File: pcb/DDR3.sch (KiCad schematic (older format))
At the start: 3 parts

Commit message: schematic completed. Time for review
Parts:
- added R?: 100, symbol R
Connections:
- net DDR3_CK_N: now also R?.2
- net DDR3_CK_P: now also R?.1
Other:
- moved on the sheet: R?, U?A

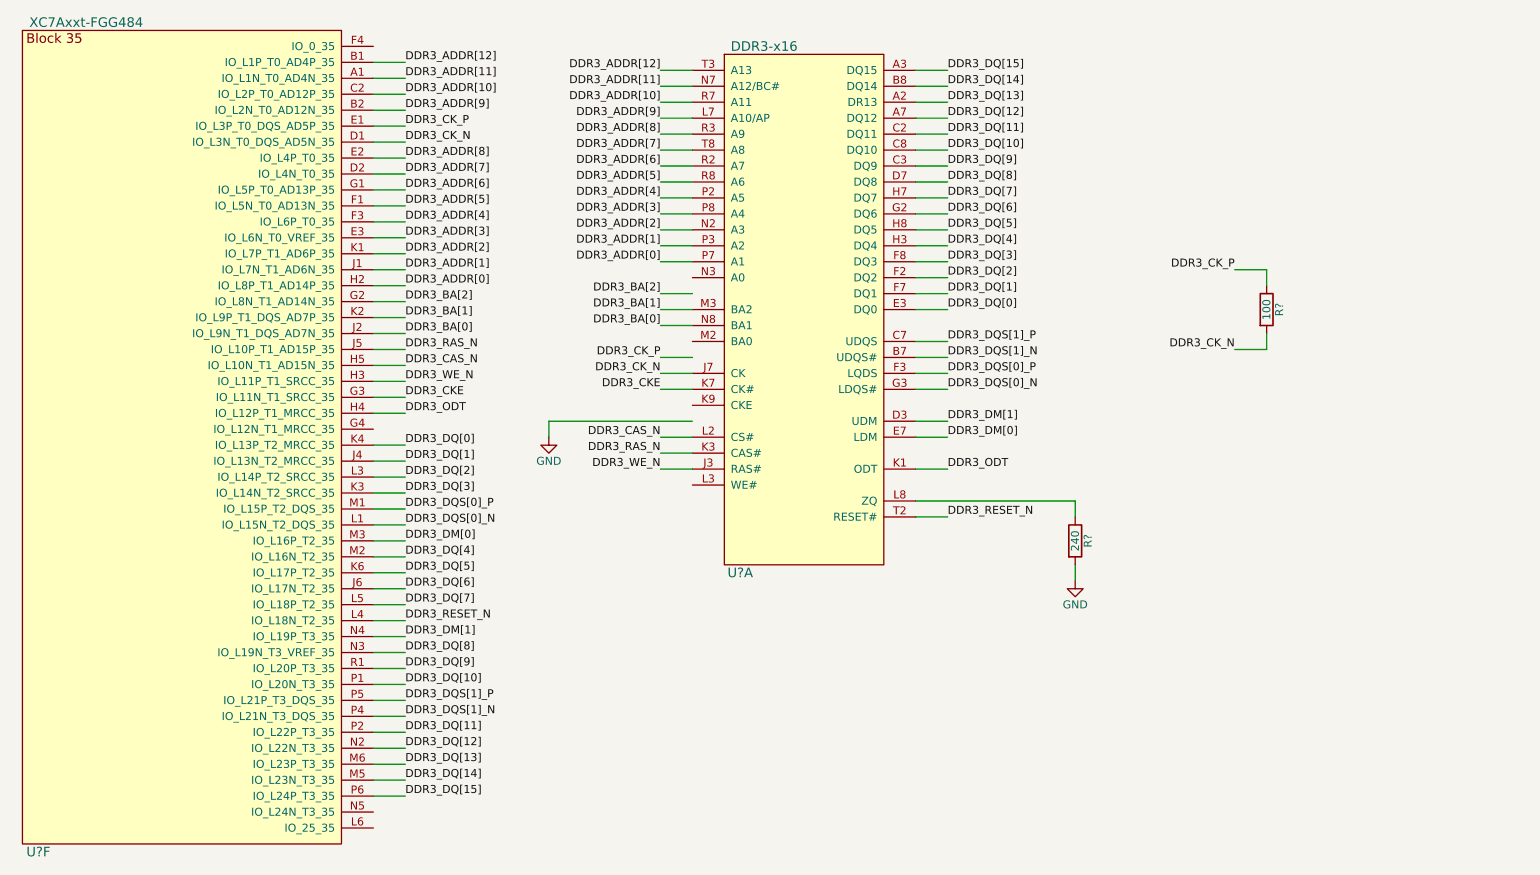
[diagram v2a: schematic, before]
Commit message: Added part numbers and updated schematic
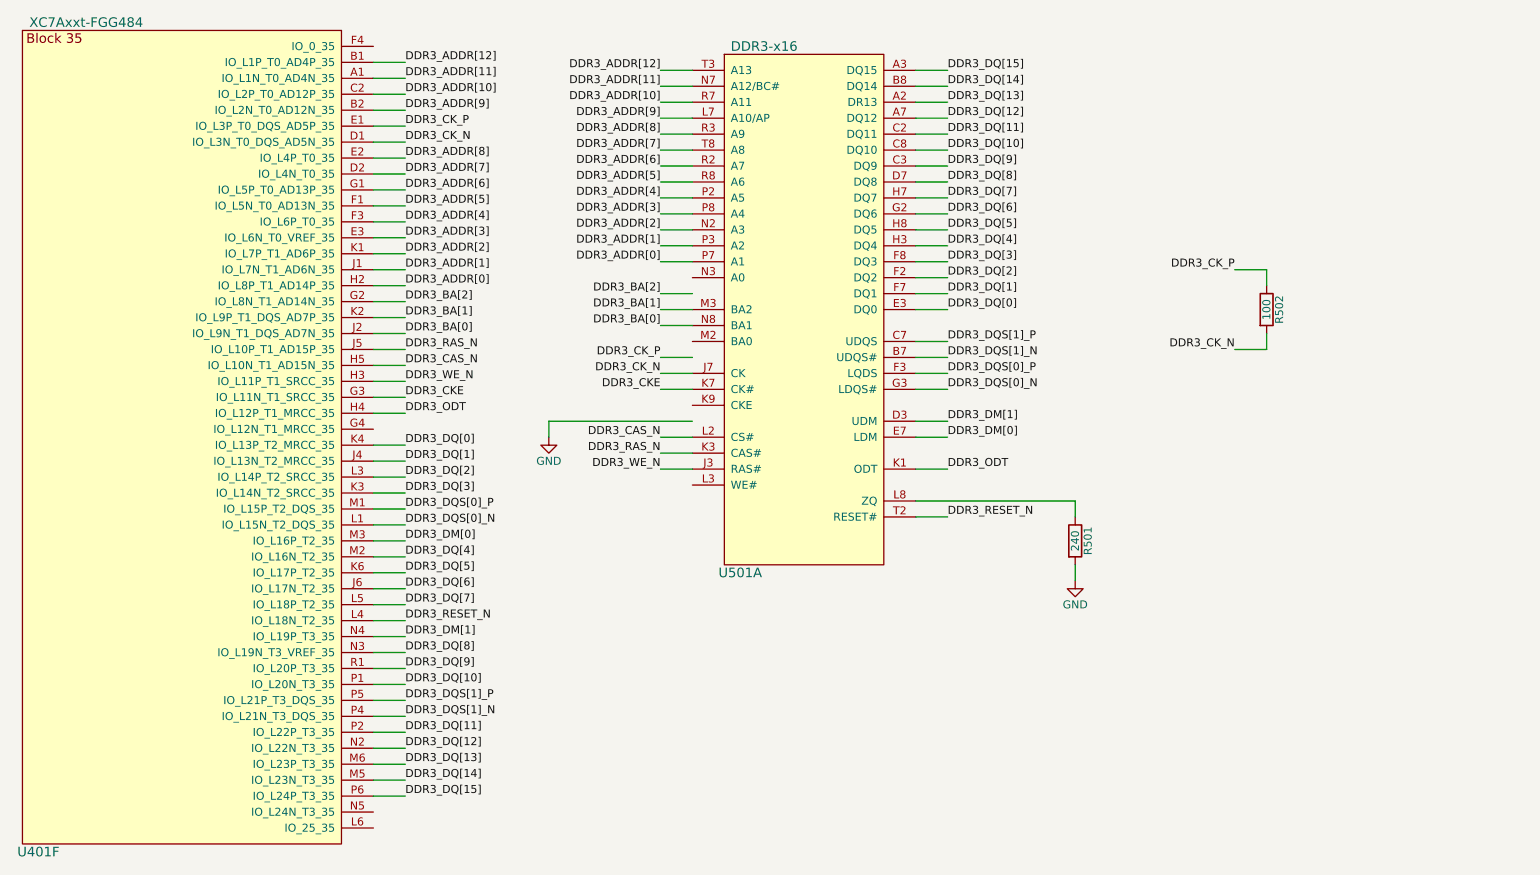
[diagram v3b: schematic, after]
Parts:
- gave numbers to parts that had none: 4
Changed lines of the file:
@@
 $EndDescr
 $Comp
-L XC7Axxt-FGG484 U?
+L XC7Axxt-FGG484 U401
 U 6 1 561B1A23
 P 2200 3450
-F 0 "U?" H 1300 850 60  0000 C CNN
+F 0 "U401" H 1300 850 60  0000 C CNN
 F 1 "XC7Axxt-FGG484" H 1600 6050 60  0000 C CNN
 F 2 "" H 2200 3500 60  0000 C CNN
@@
 DDR3_RESET_N
 $Comp
-L R R?
+L R R501
 U 1 1 561B3879
 P 7800 4100
-F 0 "R?" V 7880 4100 50  0000 C CNN
+F 0 "R501" V 7880 4100 50  0000 C CNN
 F 1 "240" V 7800 4100 50  0000 C CNN
 F 2 "" V 7730 4100 30  0000 C CNN
@@
 $EndComp
 $Comp
-L GND #PWR?
+L GND #PWR501
 U 1 1 561B38E8
 P 4500 3450
-F 0 "#PWR?" H 4500 3200 50  0001 C CNN
+F 0 "#PWR501" H 4500 3200 50  0001 C CNN
 F 1 "GND" H 4500 3300 50  0000 C CNN
 F 2 "" H 4500 3450 60  0000 C CNN
@@
 $EndComp
 $Comp
-L GND #PWR?
+L GND #PWR502
 U 1 1 561B3902
 P 7800 4350
-F 0 "#PWR?" H 7800 4100 50  0001 C CNN
+F 0 "#PWR502" H 7800 4100 50  0001 C CNN
 F 1 "GND" H 7800 4200 50  0000 C CNN
 F 2 "" H 7800 4350 60  0000 C CNN
@@
 	7800 4250 7800 4350
 $Comp
-L DDR3-x16 U?
+L DDR3-x16 U501
 U 1 1 561B3C0E
 P 6100 2650
-F 0 "U?" H 5700 1000 60  0000 C CNN
+F 0 "U501" H 5700 1000 60  0000 C CNN
 F 1 "DDR3-x16" H 5850 4300 60  0000 C CNN
 F 2 "" H 6100 2250 60  0000 C CNN
@@
 	3600 3500 3400 3500
 $Comp
-L R R?
+L R R502
 U 1 1 56514DC3
 P 9000 2650
-F 0 "R?" V 9080 2650 50  0000 C CNN
+F 0 "R502" V 9080 2650 50  0000 C CNN
 F 1 "100" V 9000 2650 50  0000 C CNN
 F 2 "" V 8930 2650 30  0000 C CNN

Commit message: mostly done with component placement
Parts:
- R501, R502: footprint (none) -> wbraun_smd:R_0402
- U401: footprint (none) -> wbraun_smd:BGA_484_22x22_FULLARRAY_1MM
- U501: footprint (none) -> wbraun_smd:FBGA-96-DDR3-SDRAM
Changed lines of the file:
@@
 F 0 "U401" H 1300 850 60  0000 C CNN
 F 1 "XC7Axxt-FGG484" H 1600 6050 60  0000 C CNN
-F 2 "" H 2200 3500 60  0000 C CNN
+F 2 "wbraun_smd:BGA_484_22x22_FULLARRAY_1MM" H 2200 3500 60  0001 C CNN
 F 3 "" H 2200 3500 60  0000 C CNN
 	6    2200 3450
@@
 F 0 "R501" V 7880 4100 50  0000 C CNN
 F 1 "240" V 7800 4100 50  0000 C CNN
-F 2 "" V 7730 4100 30  0000 C CNN
+F 2 "wbraun_smd:R_0402" V 7730 4100 30  0001 C CNN
 F 3 "" H 7800 4100 30  0000 C CNN
 	1    7800 4100
@@
 $EndComp
 $Comp
-L GND #PWR501
+L GND #PWR079
 U 1 1 561B38E8
 P 4500 3450
-F 0 "#PWR501" H 4500 3200 50  0001 C CNN
+F 0 "#PWR079" H 4500 3200 50  0001 C CNN
 F 1 "GND" H 4500 3300 50  0000 C CNN
 F 2 "" H 4500 3450 60  0000 C CNN
@@
 $EndComp
 $Comp
-L GND #PWR502
+L GND #PWR080
 U 1 1 561B3902
 P 7800 4350
-F 0 "#PWR502" H 7800 4100 50  0001 C CNN
+F 0 "#PWR080" H 7800 4100 50  0001 C CNN
 F 1 "GND" H 7800 4200 50  0000 C CNN
 F 2 "" H 7800 4350 60  0000 C CNN
@@
 F 0 "U501" H 5700 1000 60  0000 C CNN
 F 1 "DDR3-x16" H 5850 4300 60  0000 C CNN
-F 2 "" H 6100 2250 60  0000 C CNN
+F 2 "wbraun_smd:FBGA-96-DDR3-SDRAM" H 6100 2250 60  0001 C CNN
 F 3 "" H 6100 2250 60  0000 C CNN
 	1    6100 2650
@@
 F 0 "R502" V 9080 2650 50  0000 C CNN
 F 1 "100" V 9000 2650 50  0000 C CNN
-F 2 "" V 8930 2650 30  0000 C CNN
+F 2 "wbraun_smd:R_0402" V 8930 2650 30  0001 C CNN
 F 3 "" H 9000 2650 30  0000 C CNN
 	1    9000 2650
